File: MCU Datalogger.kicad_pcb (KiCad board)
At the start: 2 copper layers, 52.1 x 31.7 mm, 30 parts, among them J1 Conn_01x04_Male, J2 Conn_01x09_Male, J3 Conn_01x04_Male, J4 Conn_02x03_Odd_Even, U1 24LC1025, U2 DS1337S_, U3 24LC1025, U4 ATMEGA328P-AU, Y1 32.768 MHz, Y2 16 MHz

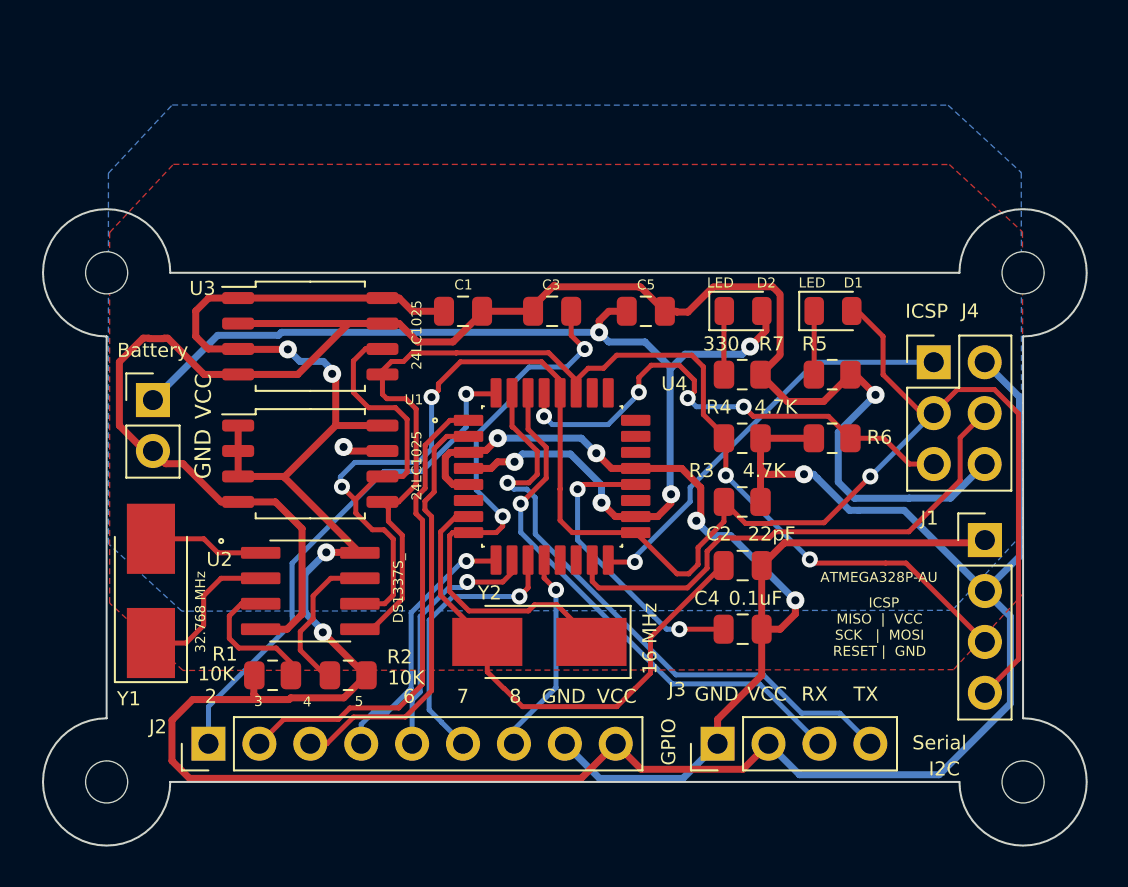
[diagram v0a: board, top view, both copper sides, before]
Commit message: Completed 2-layer PCB.
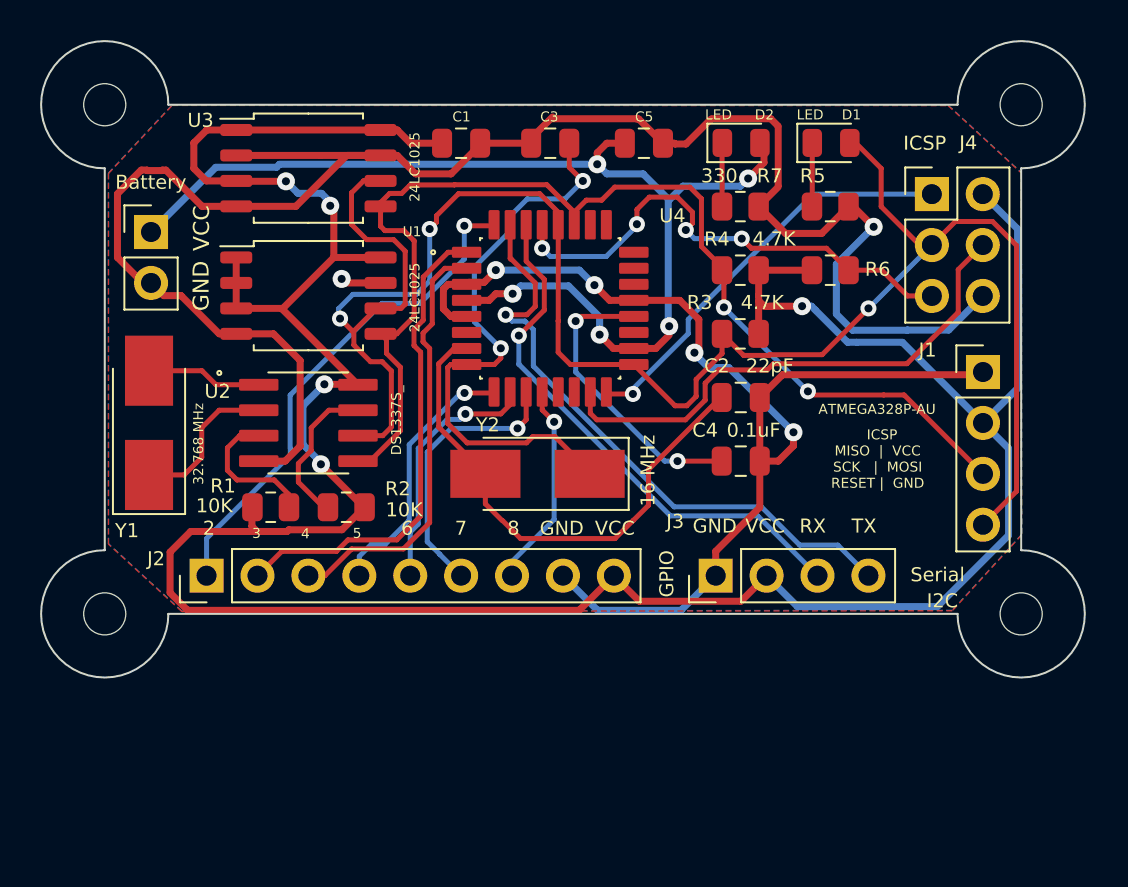
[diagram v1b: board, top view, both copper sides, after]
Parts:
- moved R1 8.39 mm to (130.1, 95.5)
- moved R2 8.39 mm to (133.9, 95.5)
- moved R5 8.39 mm to (158.0, 80.5)
- moved R7 8.39 mm to (153.5, 80.5)
- moved REF** 8.39 mm to (154.0, 79.8)
- moved U4 8.39 mm to (144.0, 85.6)
- moved BT1 8.39 mm to (124.1, 81.8)
- moved C1 8.39 mm to (139.6, 77.4)
- moved C2 8.39 mm to (153.6, 90.0)
- moved C3 8.39 mm to (144.0, 77.4)
- moved C4 8.39 mm to (153.6, 93.2)
- moved C5 8.39 mm to (148.7, 77.4)
- moved D1 8.39 mm to (158.1, 77.3)
- moved D2 8.39 mm to (153.6, 77.3)
- moved H1 8.39 mm to (121.8, 75.4)
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
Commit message: Completed 4-layer pcb routing.
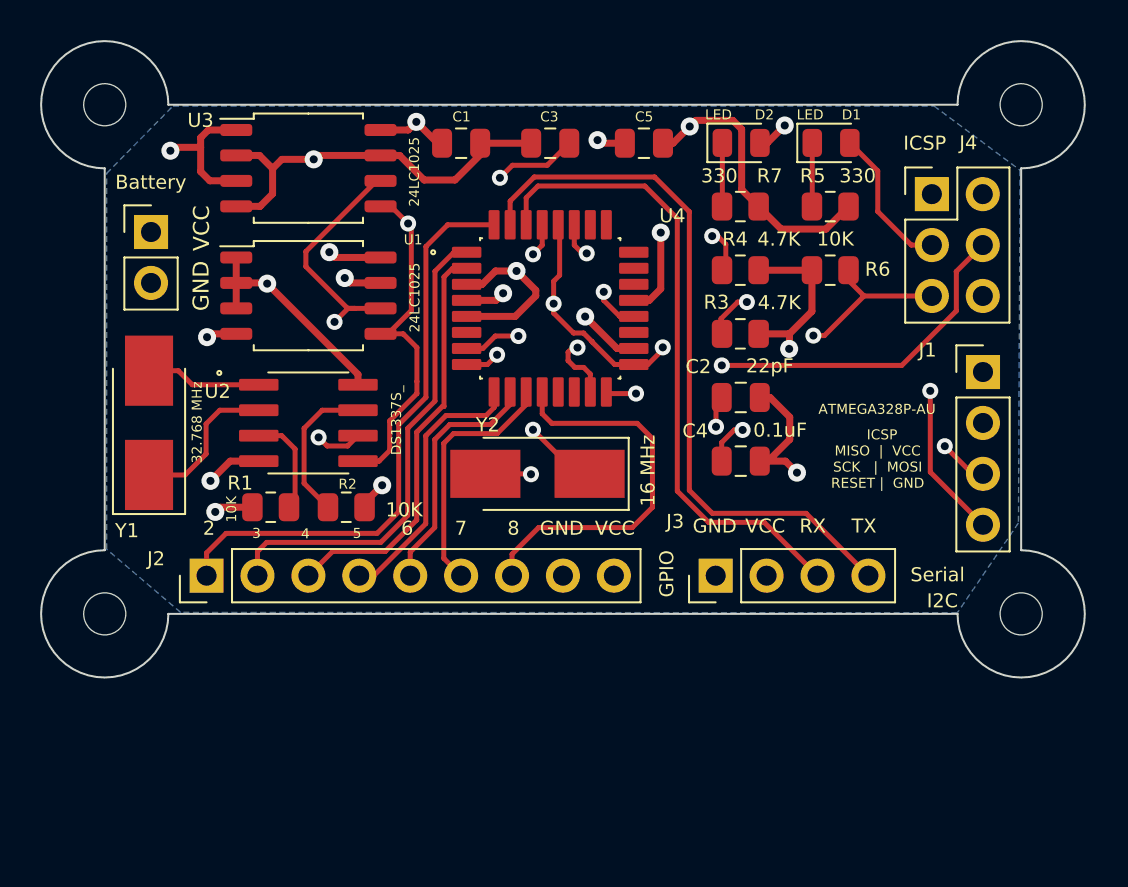
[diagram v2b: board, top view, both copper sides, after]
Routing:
- net /Vcc: track 204.7 -> 44.6 mm, vias 10 -> 11
- net GND: track 151.7 -> 60.4 mm, vias 6 -> 8
- net /SCK: track 96.1 -> 81.8 mm, vias 3 -> 6
- net /D8: track 10.3 -> 19.6 mm, vias 1 -> 0
- net Net-(C4-Pad2): track 14.7 -> 19.9 mm
- net /TX: track 30.8 -> 35.9 mm, vias 1 -> 0
- net /RX: track 27.1 -> 32.1 mm, vias 1 -> 0
- net /D2: track 25.4 -> 29.2 mm, vias 1 -> 0
- net Net-(C3-Pad2): track 29.0 -> 25.5 mm, vias 2 -> 3
- net Net-(R1-Pad2): track 7.37 -> 5.12 mm
- net /MOSI: track 26.1 -> 28.1 mm, vias 0 -> 2
- net /D7: track 13.9 -> 12.5 mm, vias 1 -> 0
- net /SDA: track 57.5 -> 56.3 mm, vias 2 -> 4
- net Net-(C2-Pad1): track 26.1 -> 24.9 mm, vias 0 -> 3
- net /RESET: track 25.5 -> 26.5 mm, vias 4 -> 2
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- added copper zone on In1.Cu, net /Vcc
- removed copper zone on F.Cu, net /Vcc
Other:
- copper layers 2 -> 4

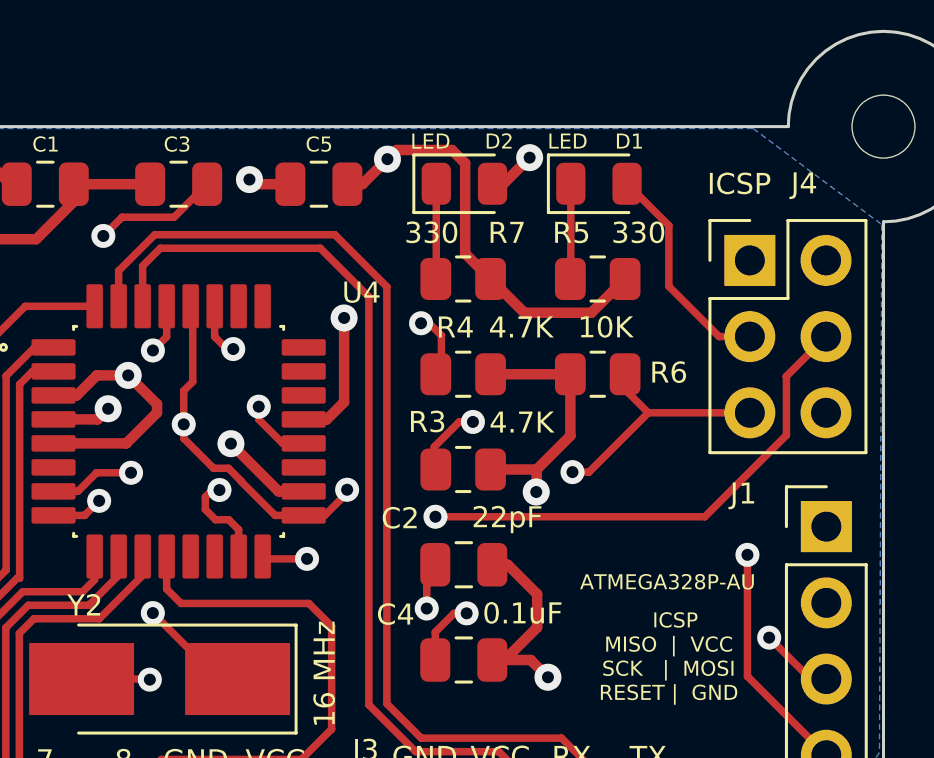
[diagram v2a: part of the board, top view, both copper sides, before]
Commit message: Fixed net bugs in 4 layer version of the PCB.
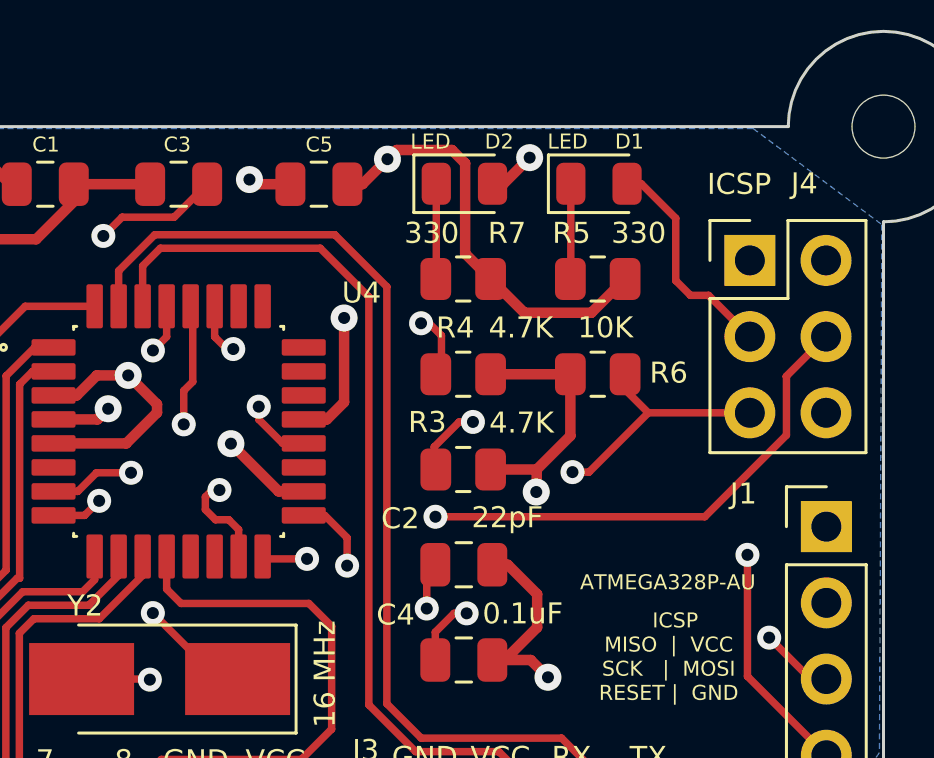
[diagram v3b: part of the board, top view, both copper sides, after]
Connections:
- J1 pad 4: /SCK -> /SCL
- R3 pad 2: /SCK -> /SCL
- U1 pad 6: /SCK -> /SCL
- U2 pad 6: /SCK -> /SCL
- U3 pad 6: /SCK -> /SCL
- U4 pad 28: /SCK -> /SCL
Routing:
- net /SCL: track 0.00 -> 69.4 mm, vias 0 -> 5
- net /SCK: track 81.8 -> 32.9 mm, vias 6 -> 1
- net /Vcc: track 44.6 -> 49.8 mm
